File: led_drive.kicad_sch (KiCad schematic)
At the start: 111 parts, among them U301 AP22653AW6-7

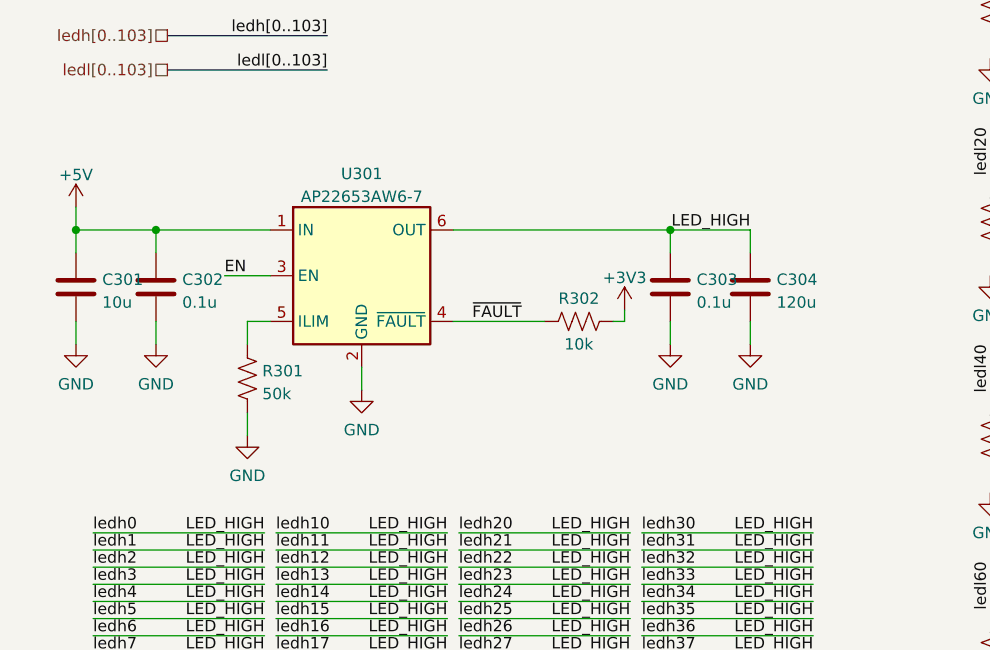
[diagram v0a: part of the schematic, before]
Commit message: Move load switch to main sheet
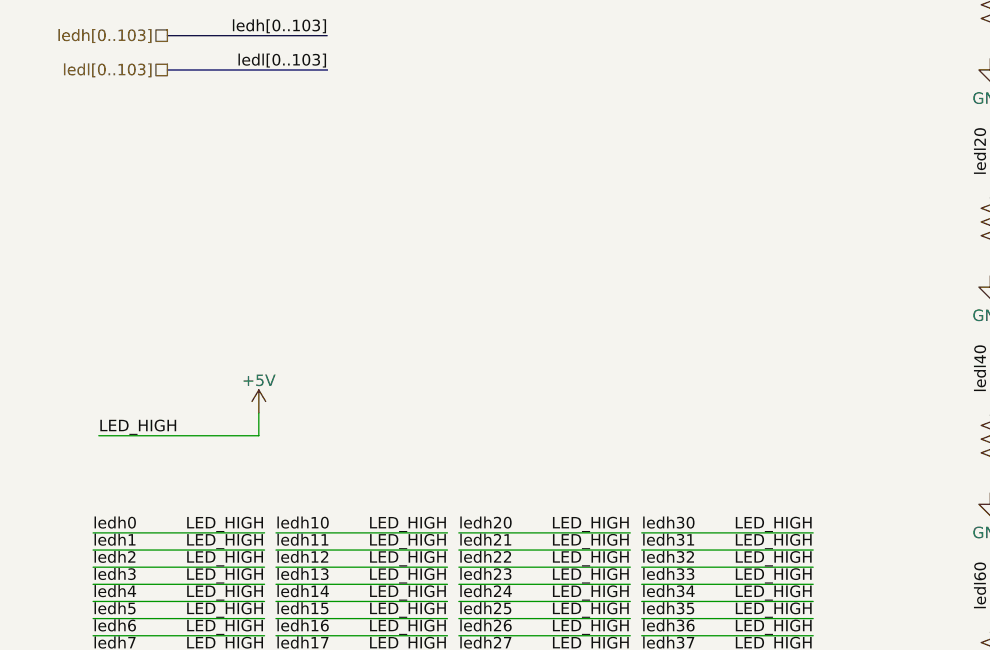
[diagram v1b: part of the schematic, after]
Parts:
- removed C301: 10u, Capacitor_SMD:C_0603_1608Metric, symbol Device:C
- removed C302, C303: 0.1u, Capacitor_SMD:C_0603_1608Metric, symbol Device:C
- removed C304: 120u, Capacitor_SMD:C_0603_1608Metric, symbol Device:C
- removed R301: 50k, Resistor_SMD:R_0603_1608Metric, symbol Device:R_US
- removed R302: 10k, Resistor_SMD:R_0603_1608Metric, symbol Device:R_US
- removed U301: AP22653AW6-7, Package_TO_SOT_SMD:SOT-23-6_Handsoldering, symbol Keyboard:AP22653AW6-7

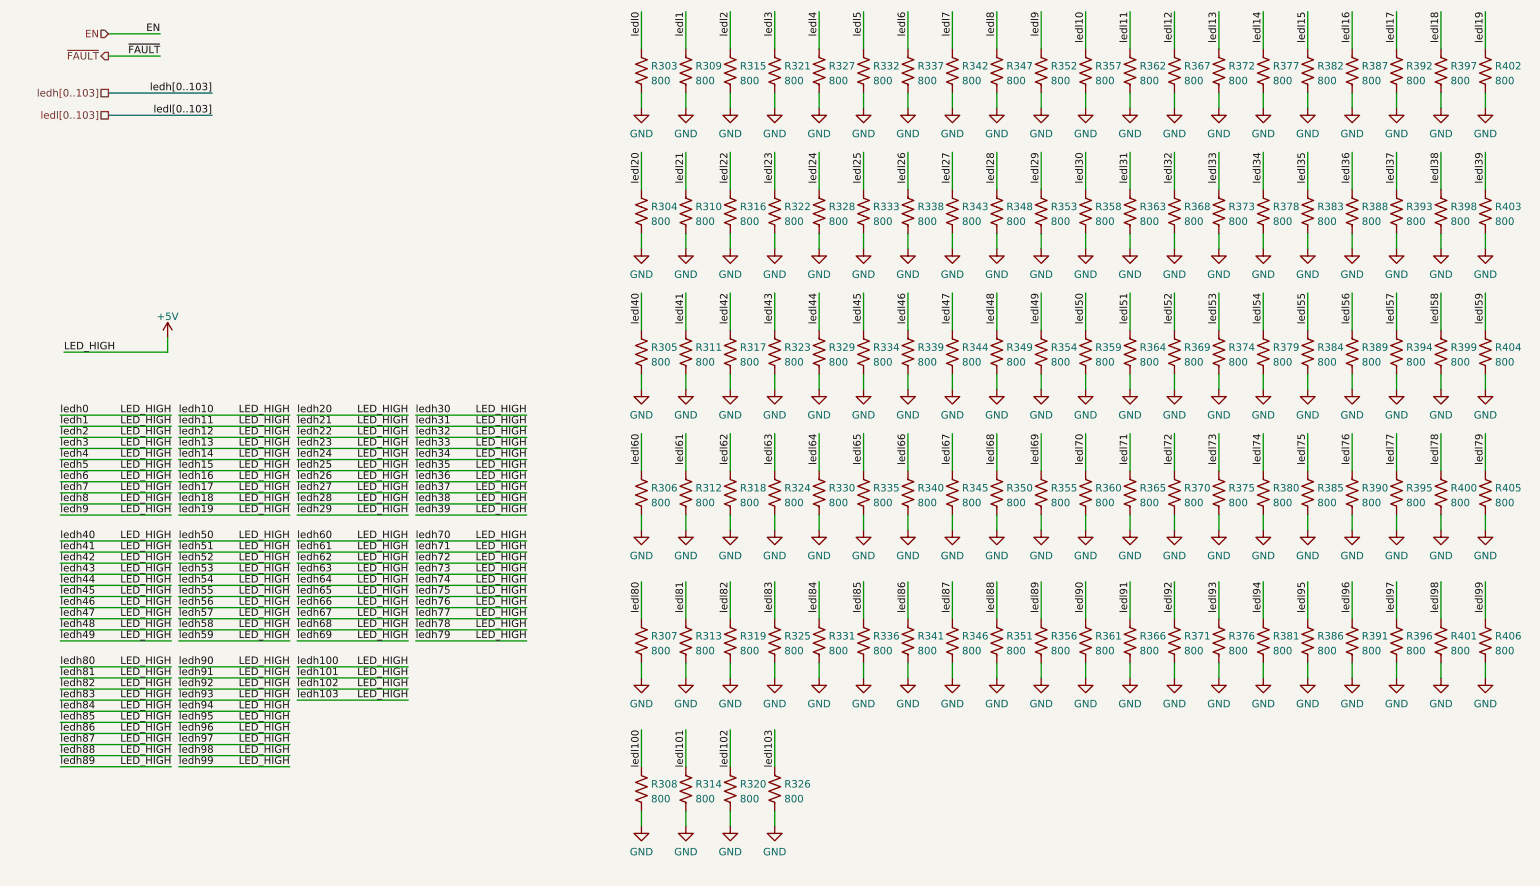
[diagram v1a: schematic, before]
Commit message: Update resistor designators to match key designators
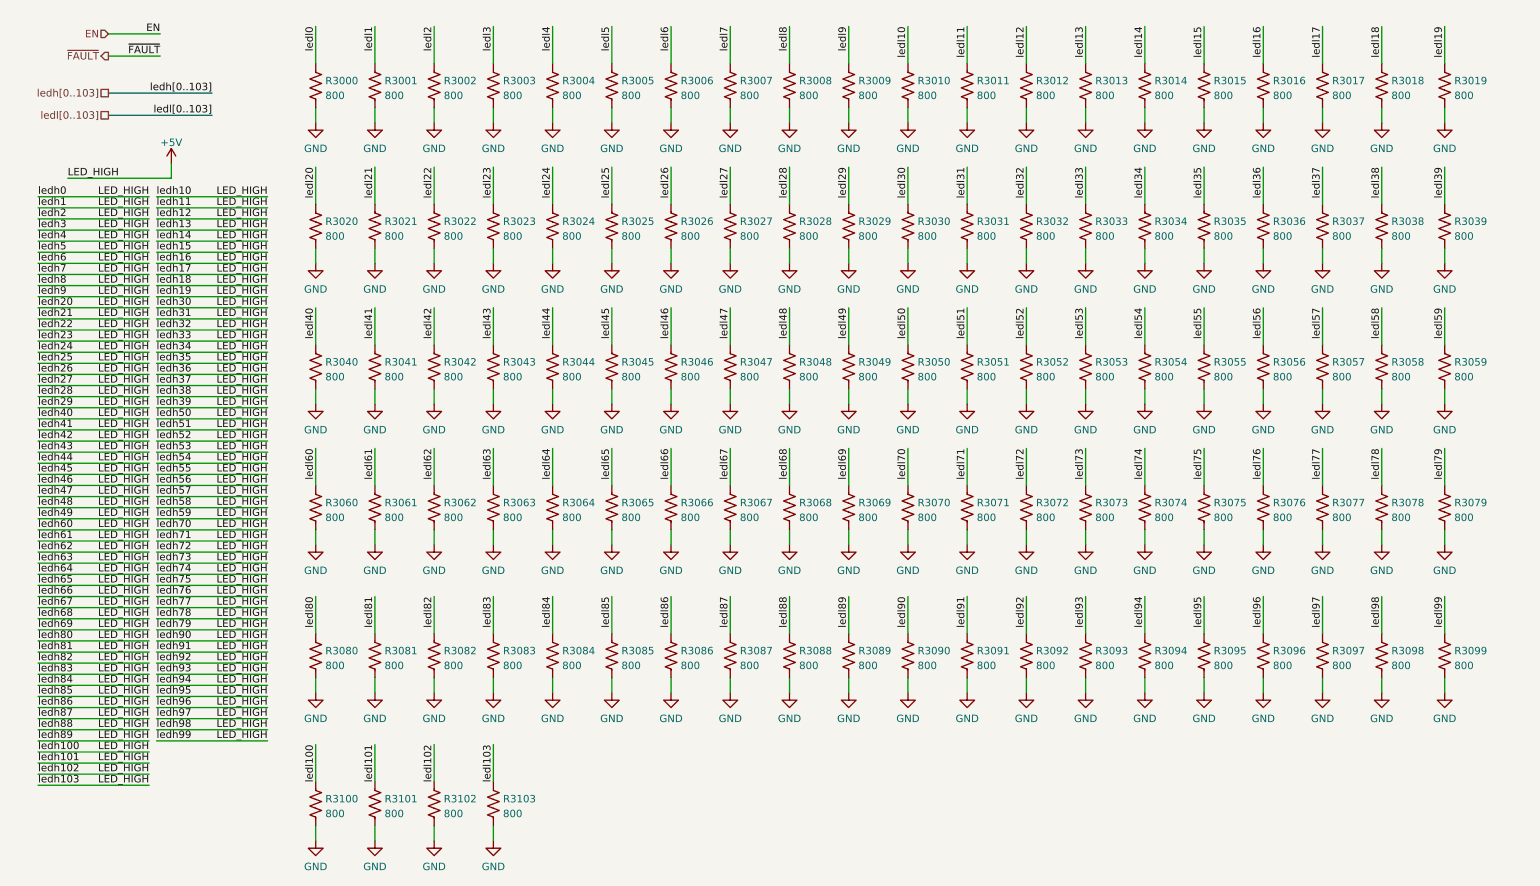
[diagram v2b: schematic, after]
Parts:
- renumbered R303 to R3000, R309 to R3001, R315 to R3002, R321 to R3003, R327 to R3004, R332 to R3005, R337 to R3006, R342 to R3007, R347 to R3008, R352 to R3009, R357 to R3010, R362 to R3011, R367 to R3012, R372 to R3013, R377 to R3014, R382 to R3015, R387 to R3016, R392 to R3017, R397 to R3018, R402 to R3019, R304 to R3020, R310 to R3021, R316 to R3022, R322 to R3023, R328 to R3024, R333 to R3025, R338 to R3026, R343 to R3027, R348 to R3028, R353 to R3029, R358 to R3030, R363 to R3031, R368 to R3032, R373 to R3033, R378 to R3034, R383 to R3035, R388 to R3036, R393 to R3037, R398 to R3038, R403 to R3039, R305 to R3040, R311 to R3041, R317 to R3042, R323 to R3043, R329 to R3044, R334 to R3045, R339 to R3046, R344 to R3047, R349 to R3048, R354 to R3049, R359 to R3050, R364 to R3051, R369 to R3052, R374 to R3053, R379 to R3054, R384 to R3055, R389 to R3056, R394 to R3057, R399 to R3058, R404 to R3059, R306 to R3060, R312 to R3061, R318 to R3062, R324 to R3063, R330 to R3064, R335 to R3065, R340 to R3066, R345 to R3067, R350 to R3068, R355 to R3069, R360 to R3070, R365 to R3071, R370 to R3072, R375 to R3073, R380 to R3074, R385 to R3075, R390 to R3076, R395 to R3077, R400 to R3078, R405 to R3079, R307 to R3080, R313 to R3081, R319 to R3082, R325 to R3083, R331 to R3084, R336 to R3085, R341 to R3086, R346 to R3087, R351 to R3088, R356 to R3089, R361 to R3090, R366 to R3091, R371 to R3092, R376 to R3093, R381 to R3094, R386 to R3095, R391 to R3096, R396 to R3097, R401 to R3098, R406 to R3099, R308 to R3100, R314 to R3101, R320 to R3102, R326 to R3103
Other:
- moved on the sheet: R3000, R3001, R3002, R3003, R3004, R3005, R3006, R3007, R3008, R3009, R3010, R3011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

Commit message: Working towards SMD LEDs
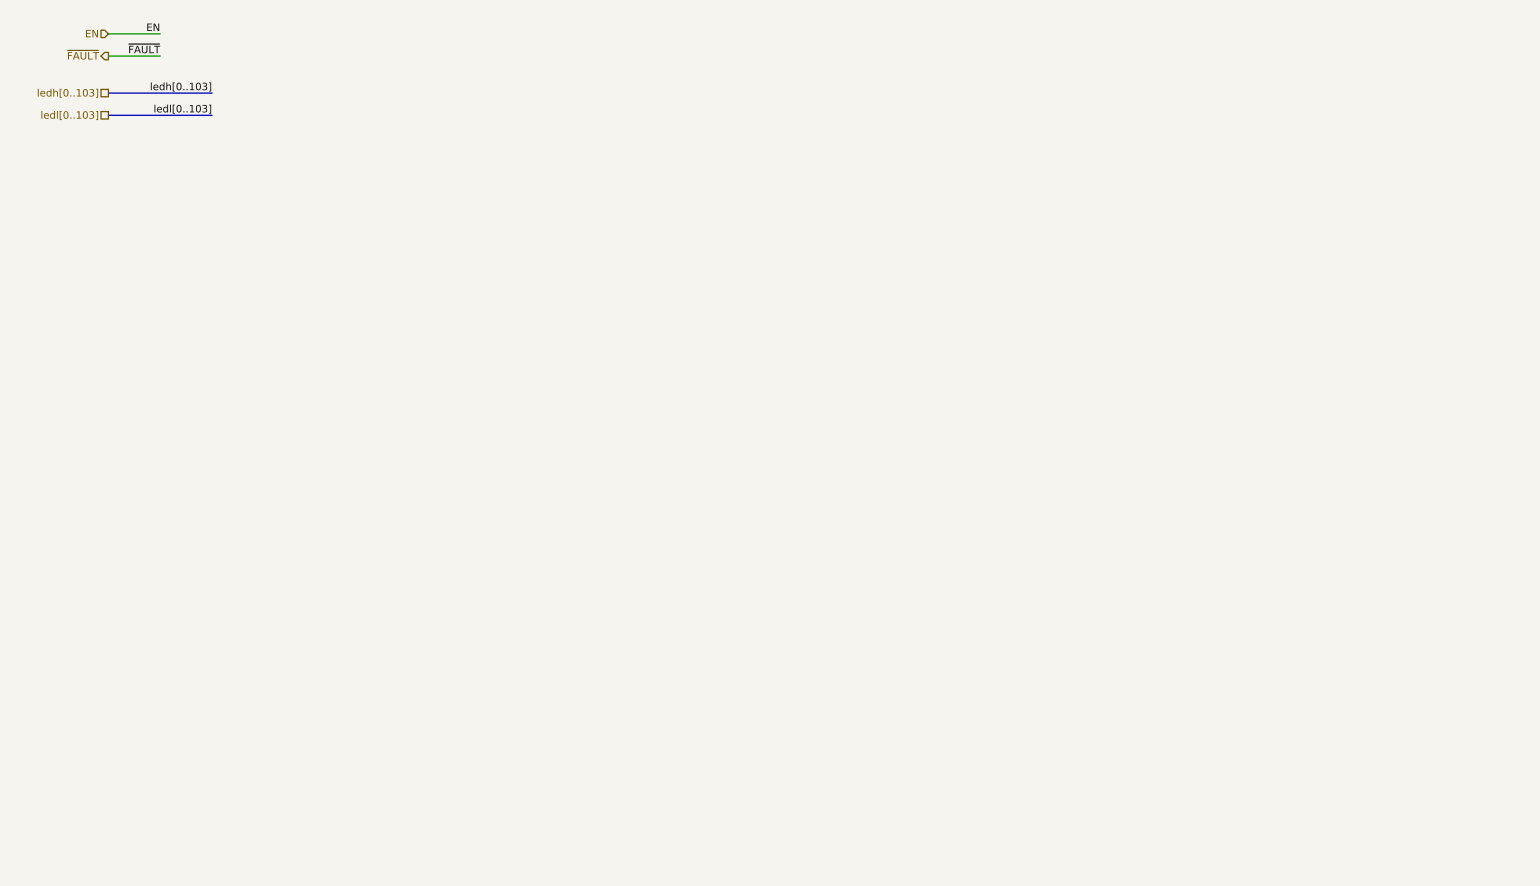
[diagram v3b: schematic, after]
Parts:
- removed R3000, R3001, R3002, R3003, R3004, R3005, R3006, R3007, R3008, R3009, R3010, R3011, R3012, R3013, R3014, R3015, R3016, R3017, R3018, R3019, R3020, R3021, R3022, R3023, R3024, R3025, R3026, R3027, R3028, R3029, R3030, R3031, R3032, R3033, R3034, R3035, R3036, R3037, R3038, R3039, R3040, R3041, R3042, R3043, R3044, R3045, R3046, R3047, R3048, R3049, R3050, R3051, R3052, R3053, R3054, R3055, R3056, R3057, R3058, R3059, R3060, R3061, R3062, R3063, R3064, R3065, R3066, R3067, R3068, R3069, R3070, R3071, R3072, R3073, R3074, R3075, R3076, R3077, R3078, R3079, R3080, R3081, R3082, R3083, R3084, R3085, R3086, R3087, R3088, R3089, R3090, R3091, R3092, R3093, R3094, R3095, R3096, R3097, R3098, R3099, R3100, R3101, R3102, R3103: 800, Resistor_SMD:R_0603_1608Metric, symbol Device:R_US

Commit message: Fleshed out layout
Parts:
- added C301, C302, C303, C304, C305, C306: 1u, Capacitor_SMD:C_0603_1608Metric, symbol Device:C
- added C307, C316: 1n, Capacitor_SMD:C_0603_1608Metric, symbol Device:C
- added U301, U302: LP5860, Package_DFN_QFN:QFN-40-1EP_5x5mm_P0.4mm_EP3.8x3.8mm_ThermalVias, symbol Keyboard:LP5860
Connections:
- new net: C304.1, U301.32 (VCAP)
- new net: C306.1, U302.32 (VCAP)
- new net +3V3: U301.37 (ADDR0_MISO), U301.38 (ADDR1_SS), U302.37 (ADDR0_MISO), U302.38 (ADDR1_SS)
- new net +5V: C301.1, C302.1, C303.1, C305.1, U301.16 (VLED), U301.40 (VCC), U302.16 (VLED), U302.40 (VCC)
- new net CS0: U301.1 (CS0)
- new net CS1: U301.2 (CS1)
- new net CS10: U301.23 (CS10)
- new net CS11: U301.24 (CS11)
- new net CS12: U301.25 (CS12)
- new net CS13: U301.26 (CS13)
- new net CS14: U301.27 (CS14)
- new net CS15: U301.28 (CS15)
- new net CS16: U301.29 (CS16)
- new net CS17: U301.30 (CS17)
- new net CS18: U302.1 (CS0)
- new net CS19: U302.2 (CS1)
- new net CS2: U301.3 (CS2)
- new net CS20: U302.3 (CS2)
- new net CS21: U302.4 (CS3)
- new net CS22: U302.5 (CS4)
- new net CS23: U302.6 (CS5)
- new net CS24: U302.7 (CS6)
- new net CS25: U302.8 (CS7)
- new net CS26: U302.9 (CS8)
- new net CS27: U302.22 (CS9)
- new net CS28: U302.23 (CS10)
- new net CS29: U302.24 (CS11)
- new net CS3: U301.4 (CS3)
- new net CS30: U302.25 (CS12)
- new net CS31: U302.26 (CS13)
- new net CS32: U302.27 (CS14)
- new net CS33: U302.28 (CS15)
- new net CS34: U302.29 (CS16)
- new net CS35: U302.30 (CS17)
- new net CS4: U301.5 (CS4)
- new net CS5: U301.6 (CS5)
- new net CS6: U301.7 (CS6)
- new net CS7: U301.8 (CS7)
- new net CS8: U301.9 (CS8)
- new net CS9: U301.22 (CS9)
- new net GND: C301.2, C302.2, C303.2, C304.2, C305.2, C306.2, C307.2, C316.2, U301.31 (AGND), U301.33 (IFS), U301.41 (GND), U302.31 (AGND), U302.33 (IFS), U302.41 (GND)
- new net SCL: U301.35 (SCL_SCLK), U302.35 (SCL_SCLK)
- new net SDA: U301.36 (SDA_MOSI), U302.36 (SDA_MOSI)
- new net SW0: U301.10 (SW0)
- new net SW1: U301.11 (SW1)
- new net SW10: U301.21 (SW10)
- new net SW11: U302.10 (SW0)
- new net SW12: U302.11 (SW1)
- new net SW13: U302.12 (SW2)
- new net SW14: U302.13 (SW3)
- new net SW15: U302.14 (SW4)
- new net SW16: U302.15 (SW5)
- new net SW17: U302.17 (SW6)
- new net SW18: U302.18 (SW7)
- new net SW19: U302.19 (SW8)
- new net SW2: U301.12 (SW2)
- new net SW20: U302.20 (SW9)
- new net SW21: U302.21 (SW10)
- new net SW3: U301.13 (SW3)
- new net SW4: U301.14 (SW4)
- new net SW5: U301.15 (SW5)
- new net SW6: U301.17 (SW6)
- new net SW7: U301.18 (SW7)
- new net SW8: U301.19 (SW8)
- new net SW9: U301.20 (SW9)
- new net VIO_EN: C307.1, C316.1, U301.39 (VIO_EN), U302.39 (VIO_EN)
- new net VSYNC: U301.34 (VSYNC), U302.34 (VSYNC)
